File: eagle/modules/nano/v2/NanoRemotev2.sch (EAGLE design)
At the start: 59 parts, among them IC1 ULN2803A, IC2 ULN2803A, IC4 ULN2803A

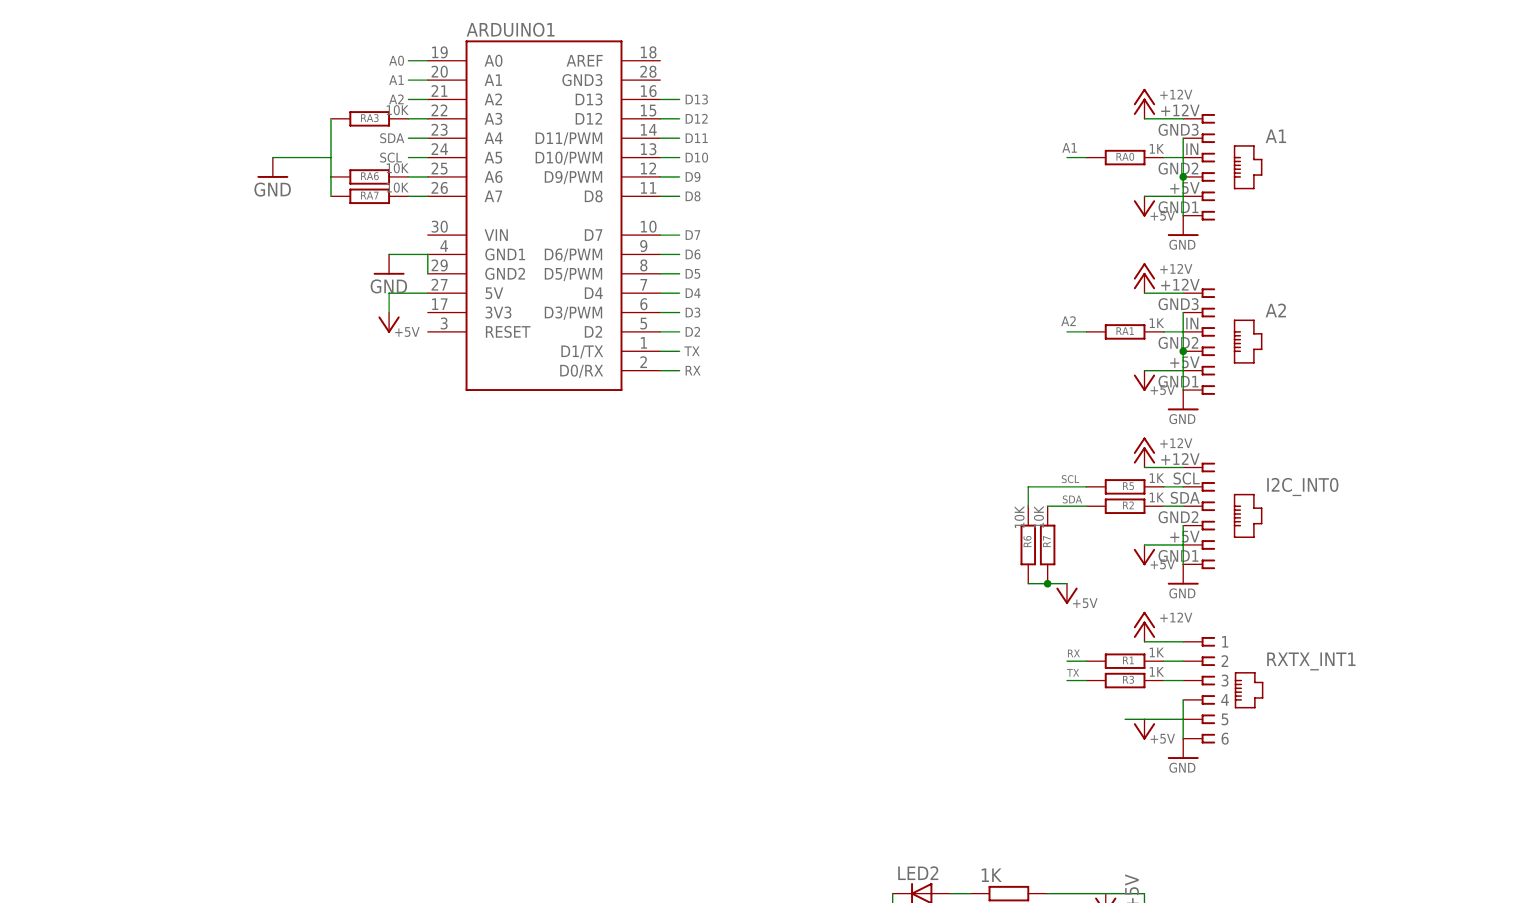
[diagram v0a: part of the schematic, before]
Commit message: New version of extension, creation of NanoEthernet (draft)
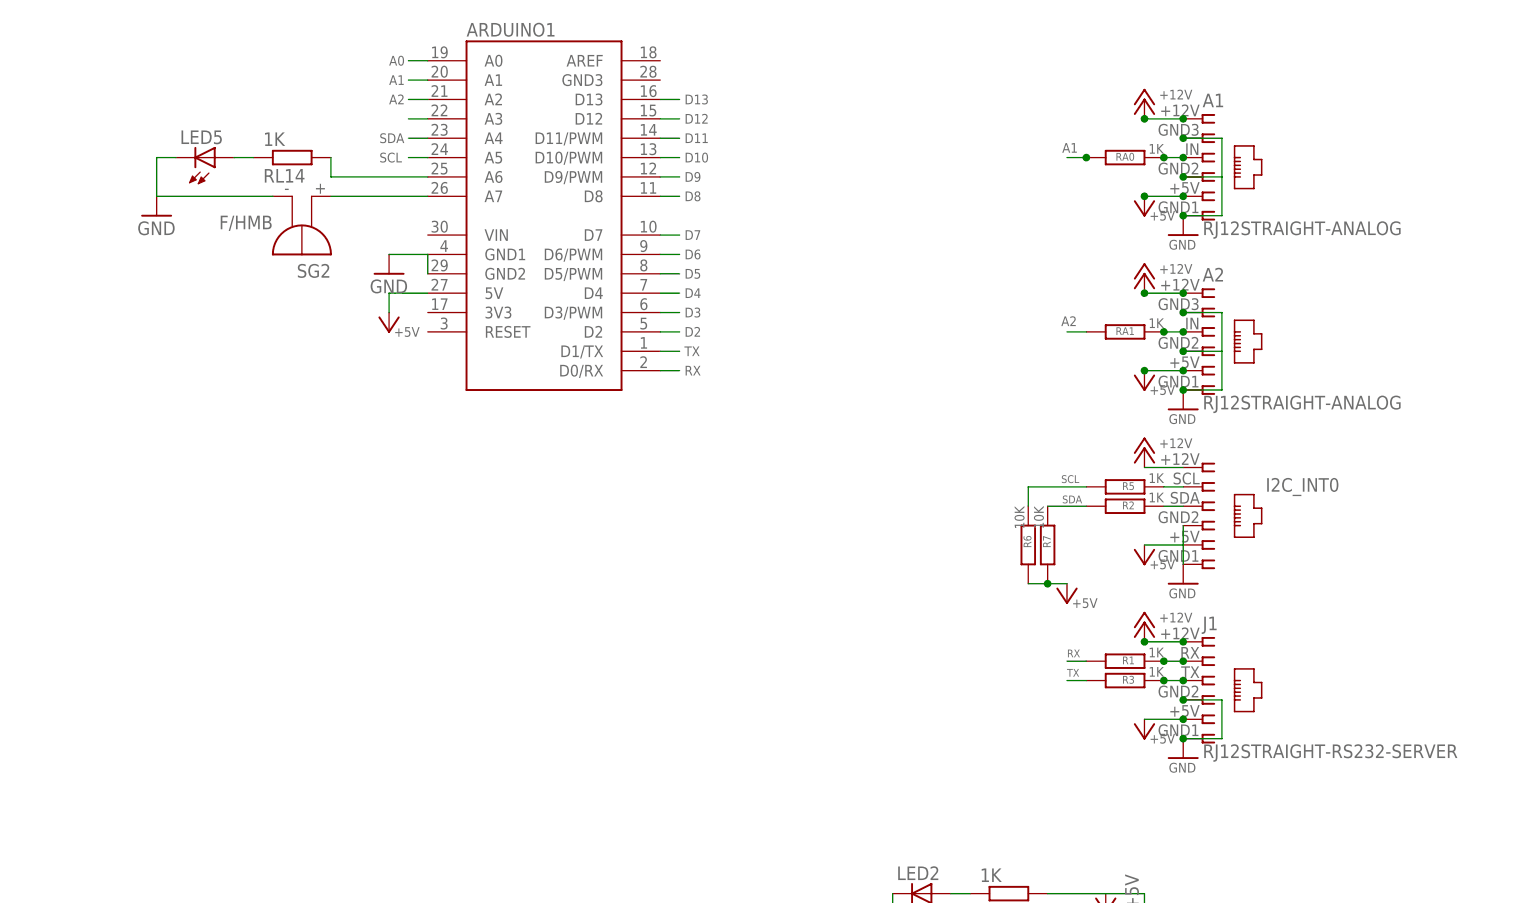
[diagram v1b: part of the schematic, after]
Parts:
- removed RA3, RA6, RA7: 10K, resistor:R-EU_M1206
- removed RXTX_INT1: RS232, lpatiny:RJ11-6XSTRAIGHT
- added J1: RJ12STRAIGHT-RS232-SERVER, lpatiny:RJ12STRAIGHT-RS232-SERVER
- added LED5: LED3MM, lpatiny:LED3MM
- added RL14: 1K, resistor:R-EU_M1206
- added SG2: F/HMB, buzzer:F/HMB
- A1: value ANALOG1 -> RJ12STRAIGHT-ANALOG; device lpatiny:RJ12 -> lpatiny:RJ12STRAIGHT-ANALOG
- A2: value ANALOG2 -> RJ12STRAIGHT-ANALOG; device lpatiny:RJ12 -> lpatiny:RJ12STRAIGHT-ANALOG
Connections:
- new net N$10: LED5.A, RL14.1
- net +12V: now also J1.1; no longer RXTX_INT1.1
- net +5V: now also J1.5; no longer RXTX_INT1.5
- net D2B5: now also J1.3; no longer RXTX_INT1.3
- net GND: now also J1.4, J1.6, LED5.C, SG2.-; no longer RA3.2, RA6.2, RA7.2, RXTX_INT1.4, RXTX_INT1.6
- net N$16: no longer RA3.1
- net N$20: now also RL14.2; no longer RA6.1
- net N$22: now also SG2.+; no longer RA7.1
- net N$7: now also J1.2; no longer RXTX_INT1.2
